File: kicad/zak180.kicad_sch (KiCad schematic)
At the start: 9 parts, among them U16 74HC00

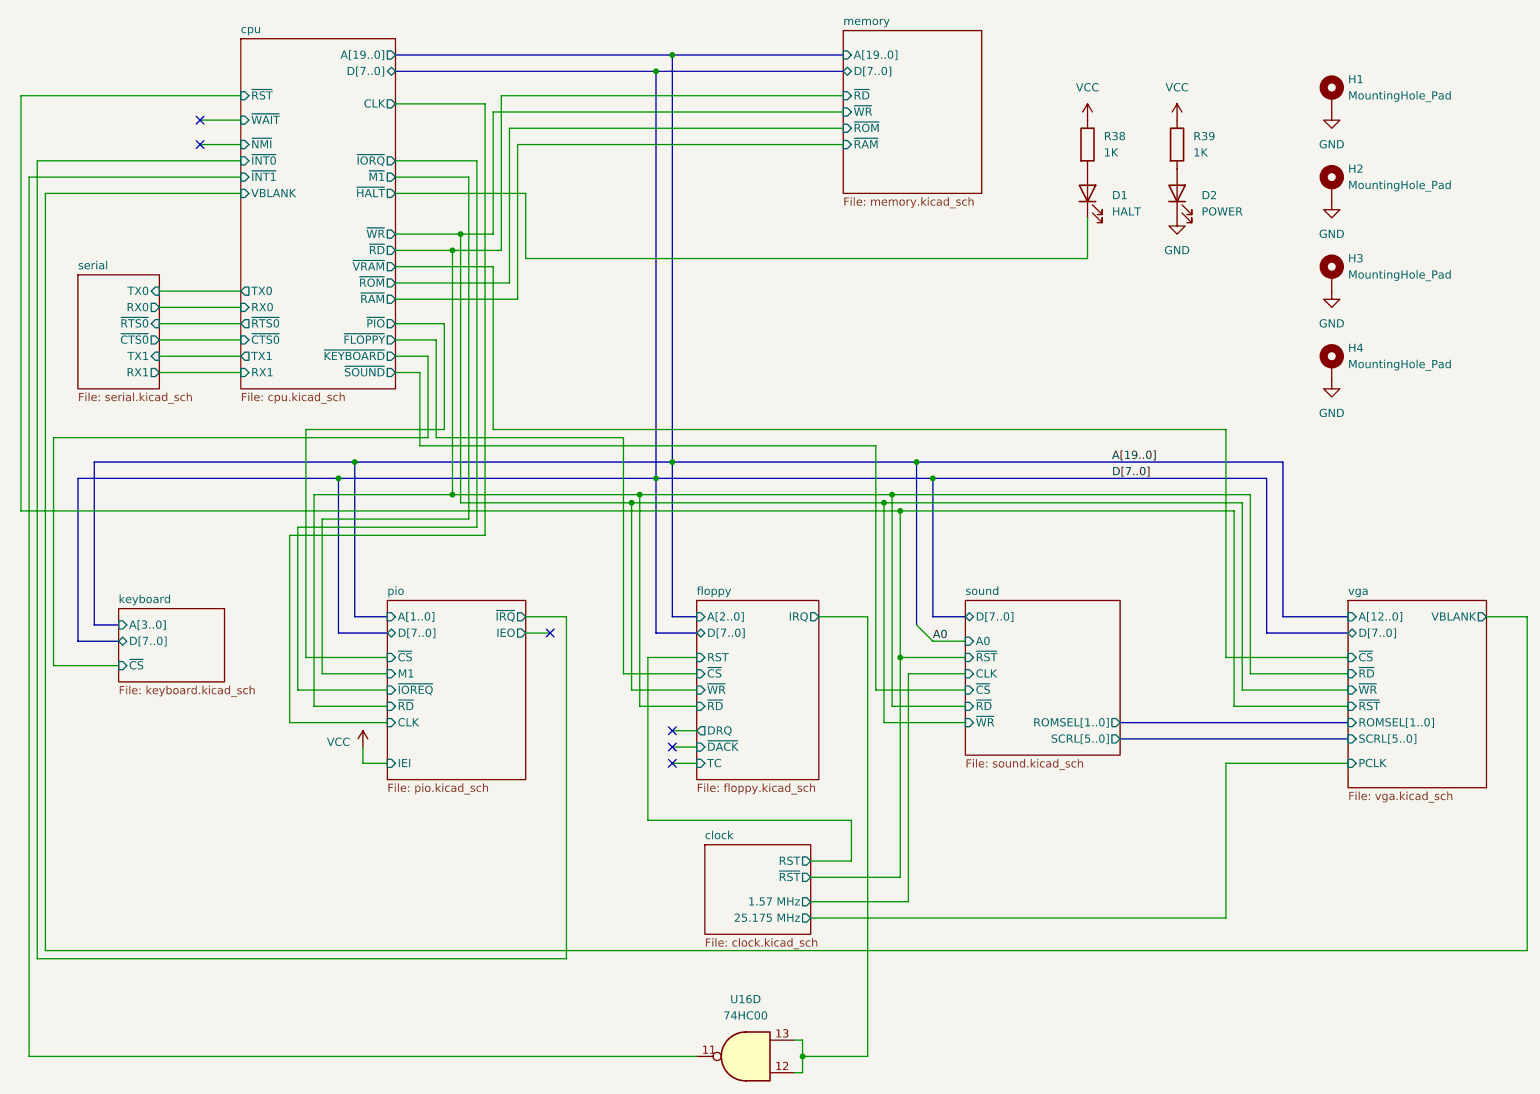
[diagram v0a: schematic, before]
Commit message: HW: Connect 82077 /DREQ to the Z180 DMA ch 1, PCB decorations
Rev B done
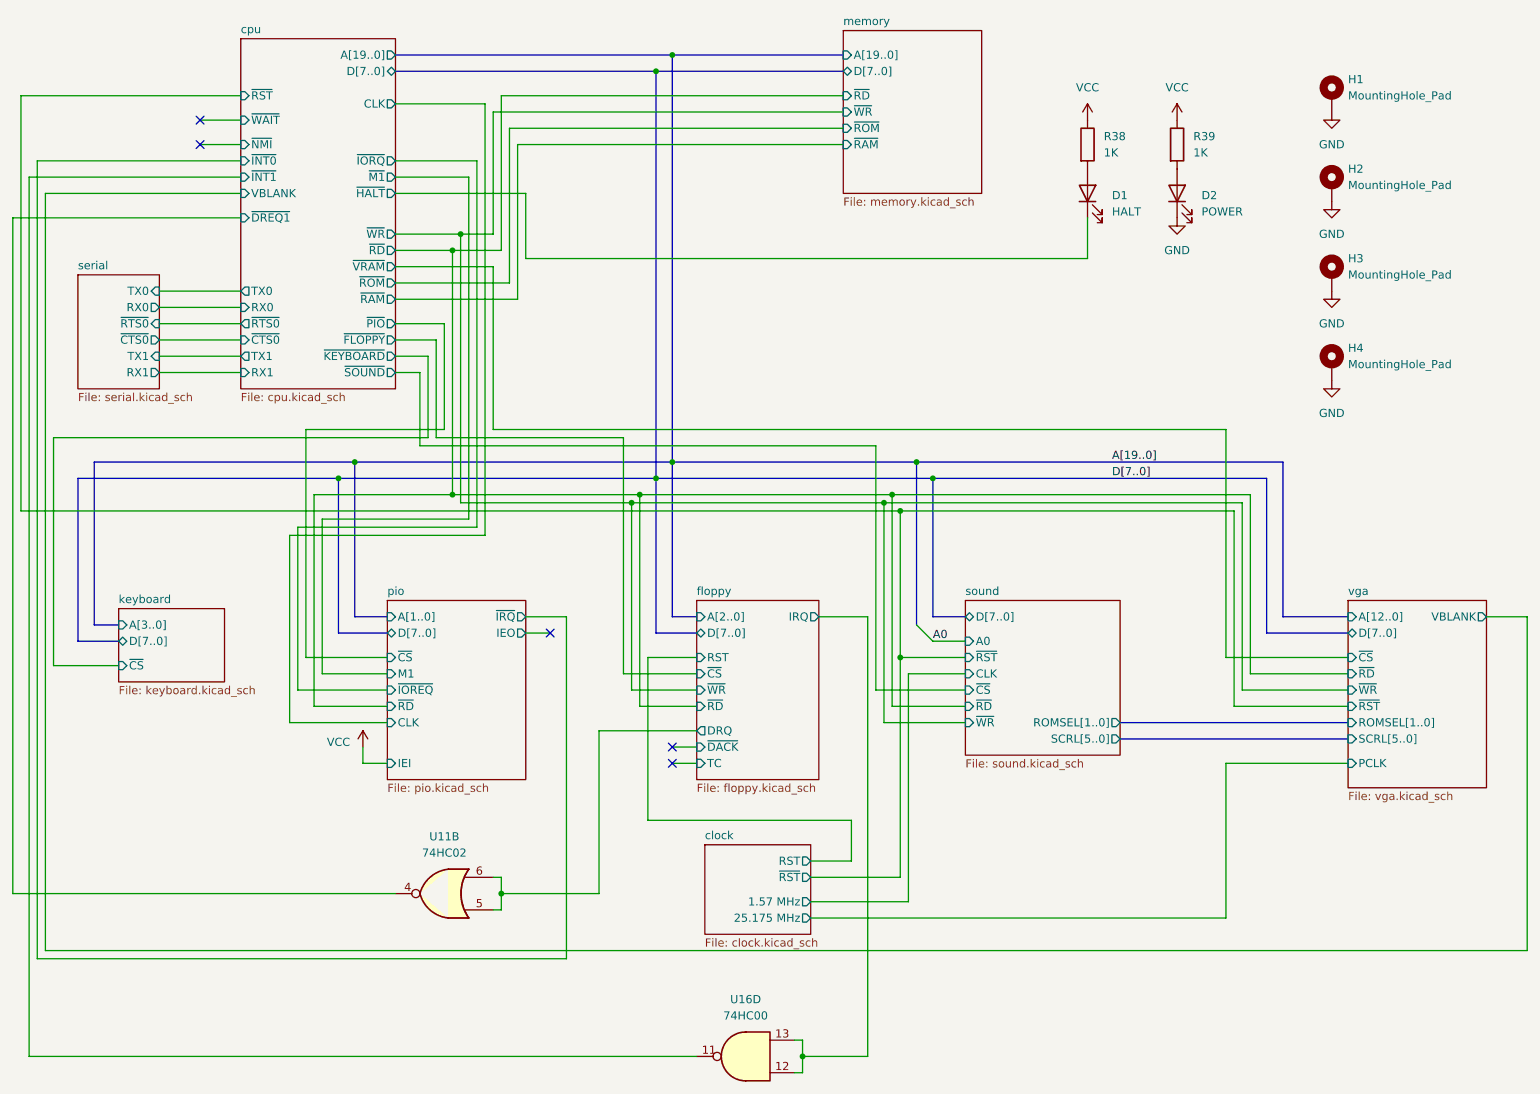
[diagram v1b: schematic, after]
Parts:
- added U11: 74HC02, Package_DIP:DIP-14_W7.62mm, symbol 74xx:74HC02
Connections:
- net floppy/DRQ: now also U11.5, U11.6
- new net cpu/~{DREQ1}: U11.4
- no-connect marks 6 -> 5
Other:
- sheet cpu ports: added ~{DREQ1}; removed none
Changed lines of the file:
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@@
 	)
 	(junction
+		(at 110.49 154.94)
+		(diameter 0)
+		(color 0 0 0 0)
+	)
+	(junction
 		(at 134.62 26.67)
 		(diameter 0)
@@
 	)
 	(no_connect
-		(at 137.16 129.54)
-	)
-	(no_connect
 		(at 63.5 34.29)
 	)
@@
 	(wire
 		(pts
+			(xy 110.49 157.48) (xy 110.49 154.94)
+		)
+		(stroke
+			(width 0)
+			(type default)
+		)
+	)
+	(wire
+		(pts
 			(xy 158.75 152.4) (xy 172.72 152.4)
 		)
@@
 	(wire
 		(pts
-			(xy 137.16 129.54) (xy 140.97 129.54)
-		)
-		(stroke
-			(width 0)
-			(type default)
-		)
-	)
-	(wire
-		(pts
 			(xy 226.06 123.19) (xy 242.57 123.19)
 		)
@@
 	(wire
 		(pts
+			(xy 125.73 154.94) (xy 110.49 154.94)
+		)
+		(stroke
+			(width 0)
+			(type default)
+		)
+	)
+	(wire
+		(pts
 			(xy 120.65 111.76) (xy 120.65 165.1)
 		)
@@
 	(wire
 		(pts
+			(xy 140.97 129.54) (xy 125.73 129.54)
+		)
+		(stroke
+			(width 0)
+			(type default)
+		)
+	)
+	(wire
+		(pts
 			(xy 157.48 182.88) (xy 157.48 180.34)
 		)
@@
 	(wire
 		(pts
+			(xy 34.29 49.53) (xy 34.29 154.94)
+		)
+		(stroke
+			(width 0)
+			(type default)
+		)
+	)
+	(wire
+		(pts
 			(xy 38.1 40.64) (xy 69.85 40.64)
 		)
@@
 	(wire
 		(pts
+			(xy 110.49 152.4) (xy 109.22 152.4)
+		)
+		(stroke
+			(width 0)
+			(type default)
+		)
+	)
+	(wire
+		(pts
 			(xy 102.87 92.71) (xy 132.08 92.71)
 		)
@@
 	(wire
 		(pts
+			(xy 110.49 154.94) (xy 110.49 152.4)
+		)
+		(stroke
+			(width 0)
+			(type default)
+		)
+	)
+	(wire
+		(pts
 			(xy 77.47 128.27) (xy 92.71 128.27)
 		)
@@
 		)
 	)
+	(wire
+		(pts
+			(xy 34.29 154.94) (xy 93.98 154.94)
+		)
+		(stroke
+			(width 0)
+			(type default)
+		)
+	)
 	(bus
 		(pts
@@
 	(wire
 		(pts
+			(xy 69.85 49.53) (xy 34.29 49.53)
+		)
+		(stroke
+			(width 0)
+			(type default)
+		)
+	)
+	(wire
+		(pts
 			(xy 109.22 82.55) (xy 223.52 82.55)
 		)
@@
 		)
 	)
+	(wire
+		(pts
+			(xy 125.73 129.54) (xy 125.73 154.94)
+		)
+		(stroke
+			(width 0)
+			(type default)
+		)
+	)
 	(bus
 		(pts
@@
 		)
 	)
+	(wire
+		(pts
+			(xy 109.22 157.48) (xy 110.49 157.48)
+		)
+		(stroke
+			(width 0)
+			(type default)
+		)
+	)
 	(bus
 		(pts
@@
 	)
 	(symbol
+		(lib_id "74xx:74HC02")
+		(at 101.6 154.94 180)
+		(unit 2)
+		(exclude_from_sim no)
+		(in_bom yes)
+		(on_board yes)
+		(dnp no)
+		(fields_autoplaced yes)
+		(property "Reference" "U11"
+			(at 101.6 146.05 0)
+			(effects
+				(font
+					(size 1.27 1.27)
+				)
+			)
+		)
+		(property "Value" "74HC02"
+			(at 101.6 148.59 0)
+			(effects
+				(font
+					(size 1.27 1.27)
+				)
+			)
+		)
+		(property "Footprint" "Package_DIP:DIP-14_W7.62mm"
+			(at 101.6 154.94 0)
+			(effects
+				(font
+					(size 1.27 1.27)
+				)
+				(hide yes)
+			)
+		)
+		(property "Datasheet" "http://www.ti.com/lit/gpn/sn74hc02"
+			(at 101.6 154.94 0)
+			(effects
+				(font
+					(size 1.27 1.27)
+				)
+				(hide yes)
+			)
+		)
+		(property "Description" "quad 2-input NOR gate"
+			(at 101.6 154.94 0)
+			(effects
+				(font
+					(size 1.27 1.27)
+				)
+				(hide yes)
+			)
+		)
+		(pin "7"
+		)
+		(pin "3"
+		)
+		(pin "5"
+		)
+		(pin "14"
+		)
+		(pin "10"
+		)
+		(pin "8"
+		)
+		(pin "4"
+		)
+		(pin "12"
+		)
+		(pin "11"
+		)
+		(pin "6"
+		)
+		(pin "1"
+		)
+		(pin "13"
+		)
+		(pin "2"
+		)
+		(pin "9"
+		)
+		(instances
+			(project "zak180"
+				(path "/ca48b56d-33a4-442b-b1b9-aaf2c2c8d68d"
+					(reference "U11")
+					(unit 2)
+				)
+			)
+		)
+	)
+	(symbol
 		(lib_id "74xx:74HC00")
 		(at 148.59 180.34 180)
@@
 			(effects
 				(font
+					(size 1.27 1.27)
+				)
+				(justify left)
+			)
+		)
+		(pin "~{DREQ1}" input
+			(at 69.85 49.53 180)
+			(effects
+				(font
